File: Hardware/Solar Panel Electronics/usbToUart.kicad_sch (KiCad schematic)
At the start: 17 parts

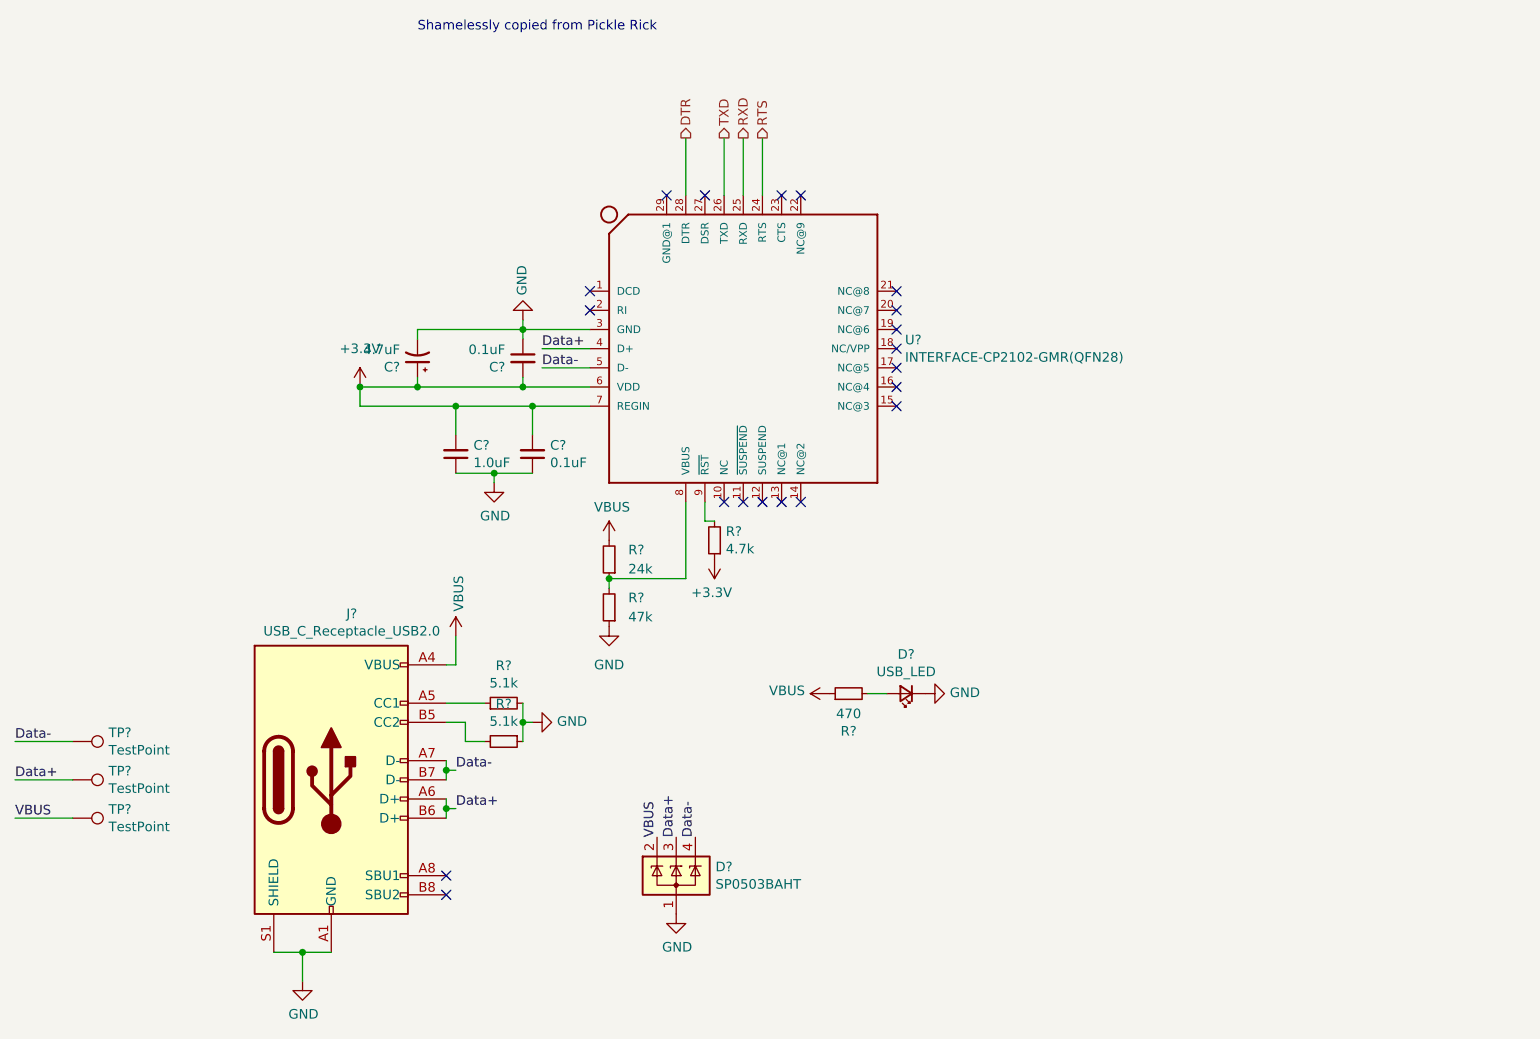
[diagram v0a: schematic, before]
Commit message: Change MCU to PICO-D4
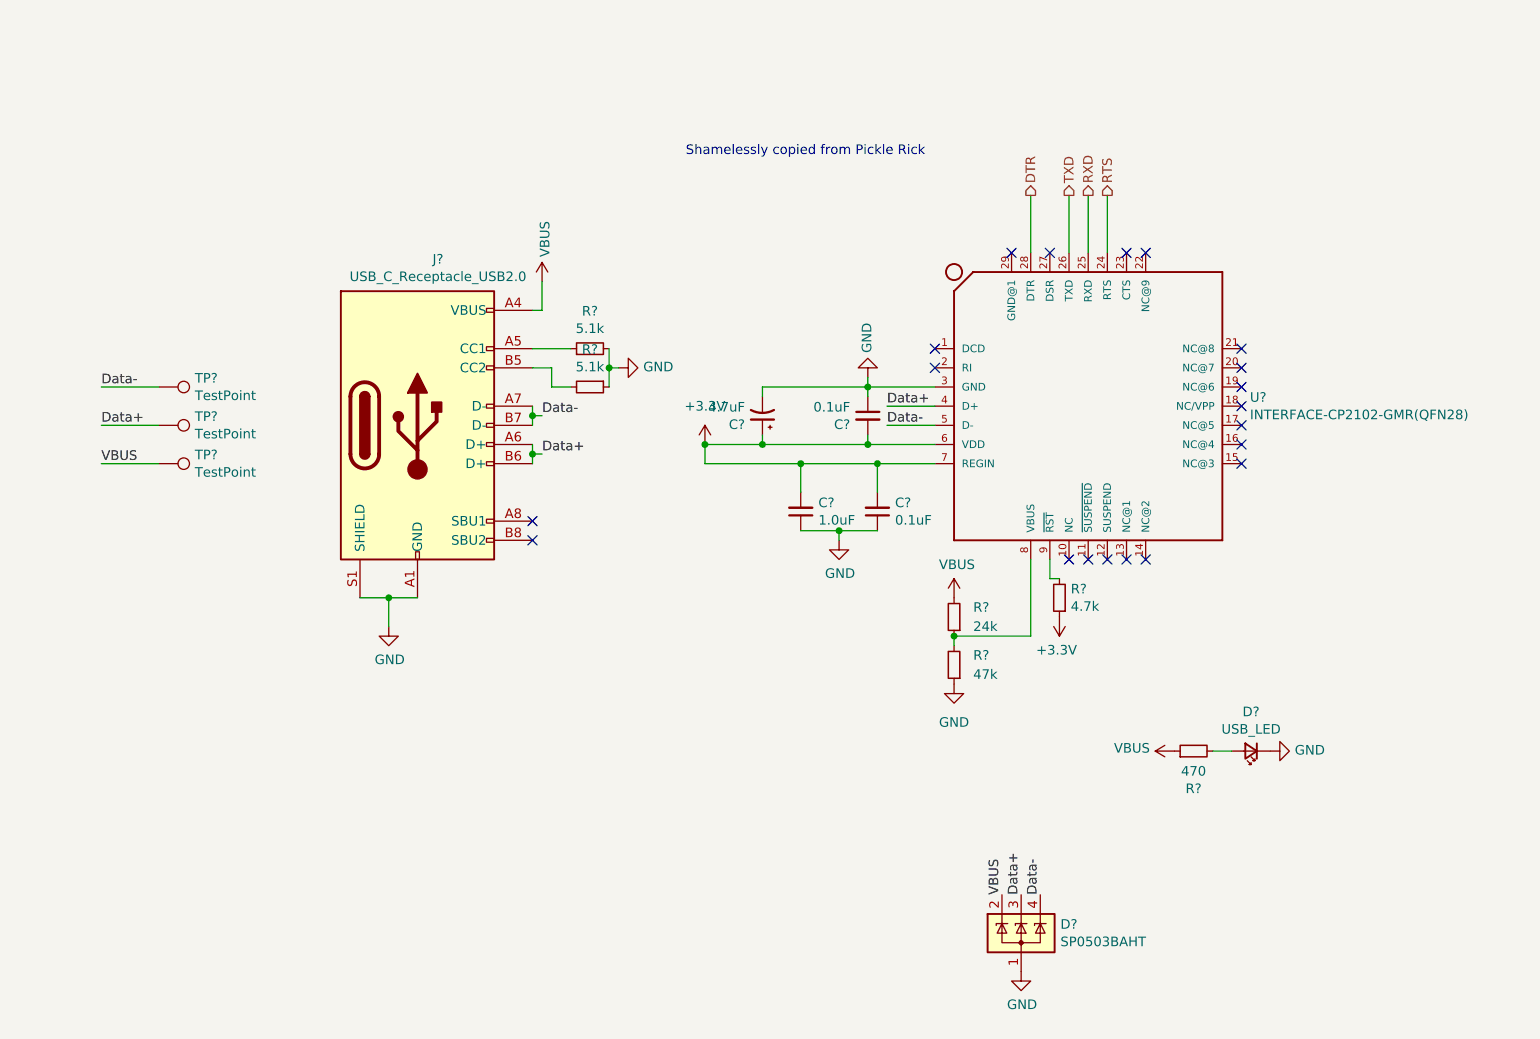
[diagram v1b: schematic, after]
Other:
- moved on the sheet: C?, D?, J?, R?, TP?, U?

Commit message: Components sized for our requirements. Added ideal diode IC LTC4411 which is more efficient than a normal diode.
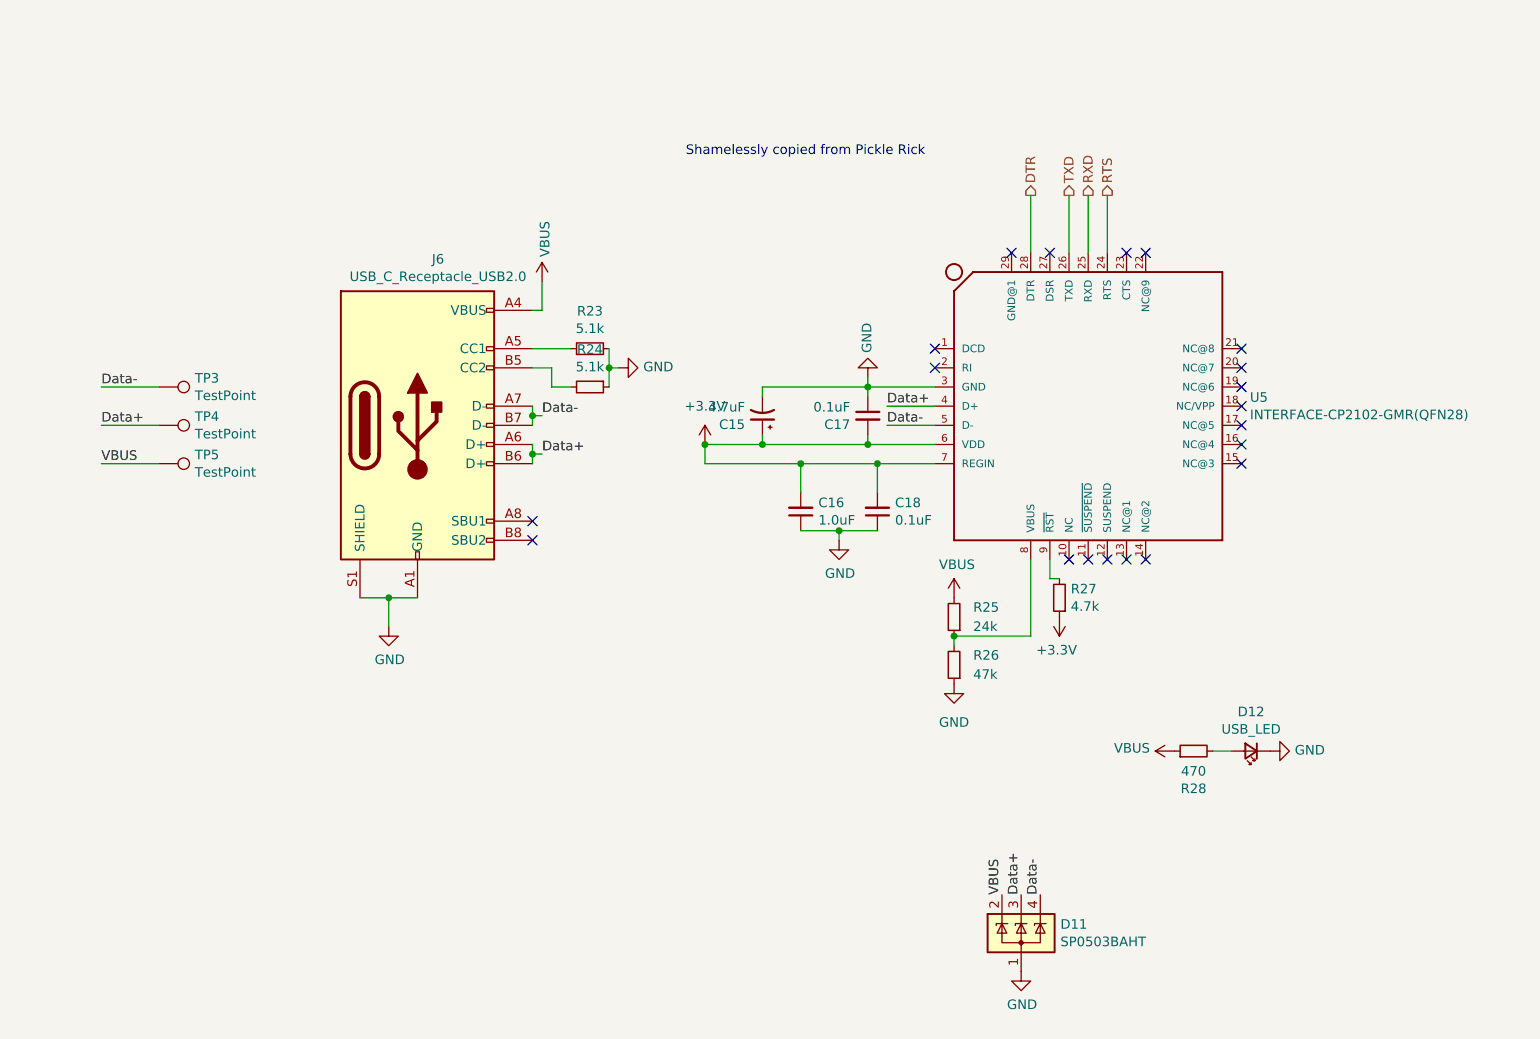
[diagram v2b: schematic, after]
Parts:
- gave numbers to parts that had none: 17
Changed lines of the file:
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@@
   (symbol (lib_id "Device:CP1_Small") (at 144.78 73.66 180) (unit 1)
     (in_bom yes) (on_board yes)
-    (property "Reference" "C?" (id 0) (at 142.4686 74.8284 0)
+    (property "Reference" "C15" (id 0) (at 142.4686 74.8284 0)
       (effects (font (size 1.27 1.27)) (justify left))
     )
@@
   (symbol (lib_id "power:VBUS") (at 170.18 97.79 0) (unit 1)
     (in_bom yes) (on_board yes)
-    (property "Reference" "#PWR?" (id 0) (at 170.18 101.6 0)
+    (property "Reference" "#PWR0126" (id 0) (at 170.18 101.6 0)
       (effects (font (size 1.27 1.27)) hide)
     )
@@
   (symbol (lib_id "power:VBUS") (at 115.57 55.88 0) (unit 1)
     (in_bom yes) (on_board yes)
-    (property "Reference" "#PWR?" (id 0) (at 115.57 59.69 0)
+    (property "Reference" "#PWR0131" (id 0) (at 115.57 59.69 0)
       (effects (font (size 1.27 1.27)) hide)
     )
@@
   (symbol (lib_id "Device:C_Small") (at 158.75 73.66 0) (unit 1)
     (in_bom yes) (on_board yes)
-    (property "Reference" "C?" (id 0) (at 156.4132 74.8284 0)
+    (property "Reference" "C17" (id 0) (at 156.4132 74.8284 0)
       (effects (font (size 1.27 1.27)) (justify right))
     )
@@
   (symbol (lib_id "power:GND") (at 95.25 101.6 0) (unit 1)
     (in_bom yes) (on_board yes)
-    (property "Reference" "#PWR?" (id 0) (at 95.25 107.95 0)
+    (property "Reference" "#PWR0130" (id 0) (at 95.25 107.95 0)
       (effects (font (size 1.27 1.27)) hide)
     )
@@
   (symbol (lib_id "power:GND") (at 179.07 147.32 0) (unit 1)
     (in_bom yes) (on_board yes)
-    (property "Reference" "#PWR?" (id 0) (at 179.07 153.67 0)
+    (property "Reference" "#PWR0123" (id 0) (at 179.07 153.67 0)
       (effects (font (size 1.27 1.27)) hide)
     )
@@
   (symbol (lib_id "Connector:TestPoint") (at 64.77 69.85 270) (unit 1)
     (in_bom yes) (on_board yes)
-    (property "Reference" "TP?" (id 0) (at 69.5452 68.6816 90)
+    (property "Reference" "TP3" (id 0) (at 69.5452 68.6816 90)
       (effects (font (size 1.27 1.27)) (justify left))
     )
@@
   (symbol (lib_id "iclr:INTERFACE-CP2102-GMR(QFN28)") (at 187.96 72.39 0) (unit 1)
     (in_bom yes) (on_board yes)
-    (property "Reference" "U?" (id 0) (at 209.3976 71.2216 0)
+    (property "Reference" "U5" (id 0) (at 209.3976 71.2216 0)
       (effects (font (size 1.27 1.27)) (justify left))
     )
@@
   (symbol (lib_id "Device:R_Small") (at 121.92 64.77 90) (unit 1)
     (in_bom yes) (on_board yes)
-    (property "Reference" "R?" (id 0) (at 121.92 59.7916 90))
+    (property "Reference" "R23" (id 0) (at 121.92 59.7916 90))
     (property "Value" "5.1k" (id 1) (at 121.92 62.103 90))
     (property "Footprint" "Resistor_SMD:R_0603_1608Metric" (id 2) (at 121.92 64.77 0)
@@
   (symbol (lib_id "Device:R_Small") (at 170.18 100.33 180) (unit 1)
     (in_bom yes) (on_board yes) (fields_autoplaced)
-    (property "Reference" "R?" (id 0) (at 172.72 99.0599 0)
+    (property "Reference" "R25" (id 0) (at 172.72 99.0599 0)
       (effects (font (size 1.27 1.27)) (justify right))
     )
@@
   (symbol (lib_id "power:GND") (at 125.73 67.31 90) (unit 1)
     (in_bom yes) (on_board yes)
-    (property "Reference" "#PWR?" (id 0) (at 132.08 67.31 0)
+    (property "Reference" "#PWR0129" (id 0) (at 132.08 67.31 0)
       (effects (font (size 1.27 1.27)) hide)
     )
@@
   (symbol (lib_id "Device:R_Small") (at 170.18 106.68 180) (unit 1)
     (in_bom yes) (on_board yes) (fields_autoplaced)
-    (property "Reference" "R?" (id 0) (at 172.72 105.4099 0)
+    (property "Reference" "R26" (id 0) (at 172.72 105.4099 0)
       (effects (font (size 1.27 1.27)) (justify right))
     )
@@
   (symbol (lib_id "Device:C_Small") (at 160.02 86.36 180) (unit 1)
     (in_bom yes) (on_board yes)
-    (property "Reference" "C?" (id 0) (at 162.3568 85.1916 0)
+    (property "Reference" "C18" (id 0) (at 162.3568 85.1916 0)
       (effects (font (size 1.27 1.27)) (justify right))
     )
@@
   (symbol (lib_id "power:GND") (at 212.09 118.11 90) (unit 1)
     (in_bom yes) (on_board yes)
-    (property "Reference" "#PWR?" (id 0) (at 218.44 118.11 0)
+    (property "Reference" "#PWR0121" (id 0) (at 218.44 118.11 0)
       (effects (font (size 1.27 1.27)) hide)
     )
@@
   (symbol (lib_id "Device:LED_Small") (at 209.55 118.11 180) (unit 1)
     (in_bom yes) (on_board yes)
-    (property "Reference" "D?" (id 0) (at 209.55 112.903 0))
+    (property "Reference" "D12" (id 0) (at 209.55 112.903 0))
     (property "Value" "USB_LED" (id 1) (at 209.55 115.2144 0))
     (property "Footprint" "LED_SMD:LED_0603_1608Metric" (id 2) (at 209.55 118.11 90)
@@
   (symbol (lib_id "power:GND") (at 170.18 109.22 0) (unit 1)
     (in_bom yes) (on_board yes) (fields_autoplaced)
-    (property "Reference" "#PWR?" (id 0) (at 170.18 115.57 0)
+    (property "Reference" "#PWR0124" (id 0) (at 170.18 115.57 0)
       (effects (font (size 1.27 1.27)) hide)
     )
@@
   (symbol (lib_id "Device:R_Small") (at 121.92 69.85 270) (unit 1)
     (in_bom yes) (on_board yes)
-    (property "Reference" "R?" (id 0) (at 121.92 64.8716 90))
+    (property "Reference" "R24" (id 0) (at 121.92 64.8716 90))
     (property "Value" "5.1k" (id 1) (at 121.92 67.183 90))
     (property "Footprint" "Resistor_SMD:R_0603_1608Metric" (id 2) (at 121.92 69.85 0)
@@
   (symbol (lib_id "Device:R_Small") (at 184.15 97.79 180) (unit 1)
     (in_bom yes) (on_board yes)
-    (property "Reference" "R?" (id 0) (at 185.6486 96.6216 0)
+    (property "Reference" "R27" (id 0) (at 185.6486 96.6216 0)
       (effects (font (size 1.27 1.27)) (justify right))
     )
@@
   (symbol (lib_id "Power_Protection:SP0503BAHT") (at 179.07 142.24 0) (unit 1)
     (in_bom yes) (on_board yes)
-    (property "Reference" "D?" (id 0) (at 184.277 141.0716 0)
+    (property "Reference" "D11" (id 0) (at 184.277 141.0716 0)
       (effects (font (size 1.27 1.27)) (justify left))
     )
@@
   (symbol (lib_id "power:GND") (at 158.75 68.58 180) (unit 1)
     (in_bom yes) (on_board yes)
-    (property "Reference" "#PWR?" (id 0) (at 158.75 62.23 0)
+    (property "Reference" "#PWR0128" (id 0) (at 158.75 62.23 0)
       (effects (font (size 1.27 1.27)) hide)
     )
@@
   (symbol (lib_id "power:+3.3V") (at 184.15 100.33 180) (unit 1)
     (in_bom yes) (on_board yes)
-    (property "Reference" "#PWR?" (id 0) (at 184.15 96.52 0)
+    (property "Reference" "#PWR0122" (id 0) (at 184.15 96.52 0)
       (effects (font (size 1.27 1.27)) hide)
     )
@@
   (symbol (lib_id "power:VBUS") (at 199.39 118.11 90) (unit 1)
     (in_bom yes) (on_board yes)
-    (property "Reference" "#PWR?" (id 0) (at 203.2 118.11 0)
+    (property "Reference" "#PWR0120" (id 0) (at 203.2 118.11 0)
       (effects (font (size 1.27 1.27)) hide)
     )
@@
   (symbol (lib_id "Connector:USB_C_Receptacle_USB2.0") (at 99.06 74.93 0) (unit 1)
     (in_bom yes) (on_board yes)
-    (property "Reference" "J?" (id 0) (at 101.7778 52.9082 0))
+    (property "Reference" "J6" (id 0) (at 101.7778 52.9082 0))
     (property "Value" "USB_C_Receptacle_USB2.0" (id 1) (at 101.7778 55.2196 0))
     (property "Footprint" "Connector_USB:USB_C_Receptacle_GCT_USB4085" (id 2) (at 102.87 74.93 0)
@@
   (symbol (lib_id "power:+3.3V") (at 137.16 77.47 0) (unit 1)
     (in_bom yes) (on_board yes) (fields_autoplaced)
-    (property "Reference" "#PWR?" (id 0) (at 137.16 81.28 0)
+    (property "Reference" "#PWR0125" (id 0) (at 137.16 81.28 0)
       (effects (font (size 1.27 1.27)) hide)
     )
@@
   (symbol (lib_id "power:GND") (at 154.94 90.17 0) (unit 1)
     (in_bom yes) (on_board yes)
-    (property "Reference" "#PWR?" (id 0) (at 154.94 96.52 0)
+    (property "Reference" "#PWR0127" (id 0) (at 154.94 96.52 0)
       (effects (font (size 1.27 1.27)) hide)
     )
@@
   (symbol (lib_id "Connector:TestPoint") (at 64.77 74.93 270) (unit 1)
     (in_bom yes) (on_board yes)
-    (property "Reference" "TP?" (id 0) (at 69.5452 73.7616 90)
+    (property "Reference" "TP4" (id 0) (at 69.5452 73.7616 90)
       (effects (font (size 1.27 1.27)) (justify left))
     )
@@
   (symbol (lib_id "Device:R_Small") (at 201.93 118.11 90) (unit 1)
     (in_bom yes) (on_board yes)
-    (property "Reference" "R?" (id 0) (at 201.93 123.0884 90))
+    (property "Reference" "R28" (id 0) (at 201.93 123.0884 90))
     (property "Value" "470" (id 1) (at 201.93 120.777 90))
     (property "Footprint" "Resistor_SMD:R_0603_1608Metric" (id 2) (at 201.93 118.11 0)
@@
   (symbol (lib_id "Device:C_Small") (at 149.86 86.36 180) (unit 1)
     (in_bom yes) (on_board yes)
-    (property "Reference" "C?" (id 0) (at 152.1968 85.1916 0)
+    (property "Reference" "C16" (id 0) (at 152.1968 85.1916 0)
       (effects (font (size 1.27 1.27)) (justify right))
     )
@@
   (symbol (lib_id "Connector:TestPoint") (at 64.77 80.01 270) (unit 1)
     (in_bom yes) (on_board yes)
-    (property "Reference" "TP?" (id 0) (at 69.5452 78.8416 90)
-      (effects (font (size 1.27 1.27)) (justify left))
-    )
+    (property "Reference" "TP5" (id 0) (at 69.5452 78.8416 90)
+      (effects (font (size 1.27 1.27)) (justify left))
+    )

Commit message: ICARUS v2
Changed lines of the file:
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@@
   (symbol (lib_id "Device:R_Small") (at 121.92 69.85 270) (unit 1)
     (in_bom yes) (on_board yes)
-    (property "Reference" "R24" (id 0) (at 121.92 64.8716 90))
+    (property "Reference" "R24" (id 0) (at 121.7676 66.3956 90))
     (property "Value" "5.1k" (id 1) (at 121.92 67.183 90))
     (property "Footprint" "Resistor_SMD:R_0603_1608Metric" (id 2) (at 121.92 69.85 0)
